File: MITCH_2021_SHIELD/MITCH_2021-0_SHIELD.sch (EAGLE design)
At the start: 1 part, among them U1 NUCLEO-F401RE-BOTTOM

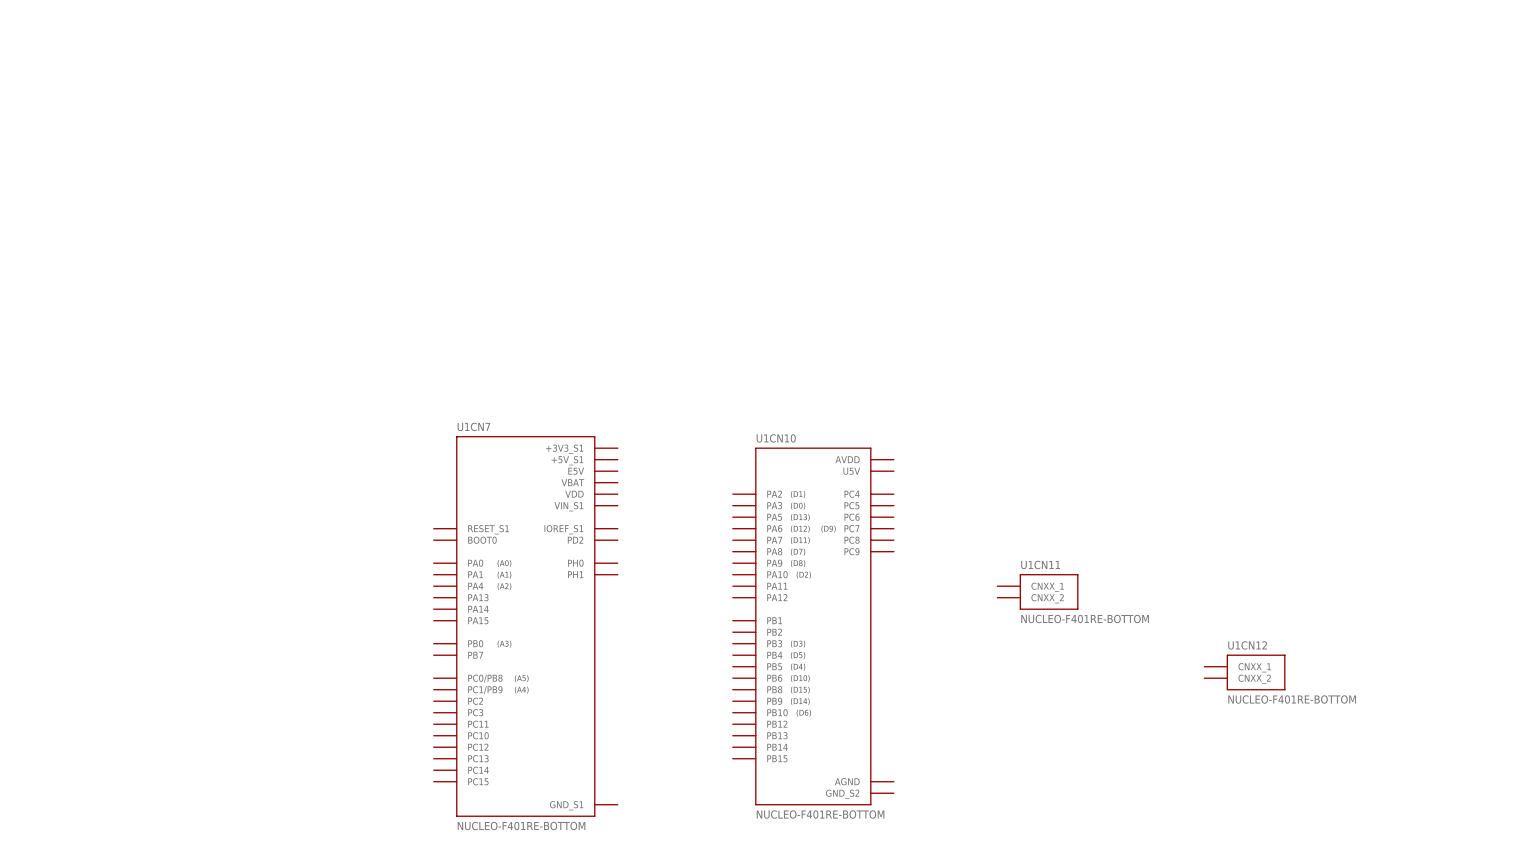
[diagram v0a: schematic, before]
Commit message: updated shield schematic
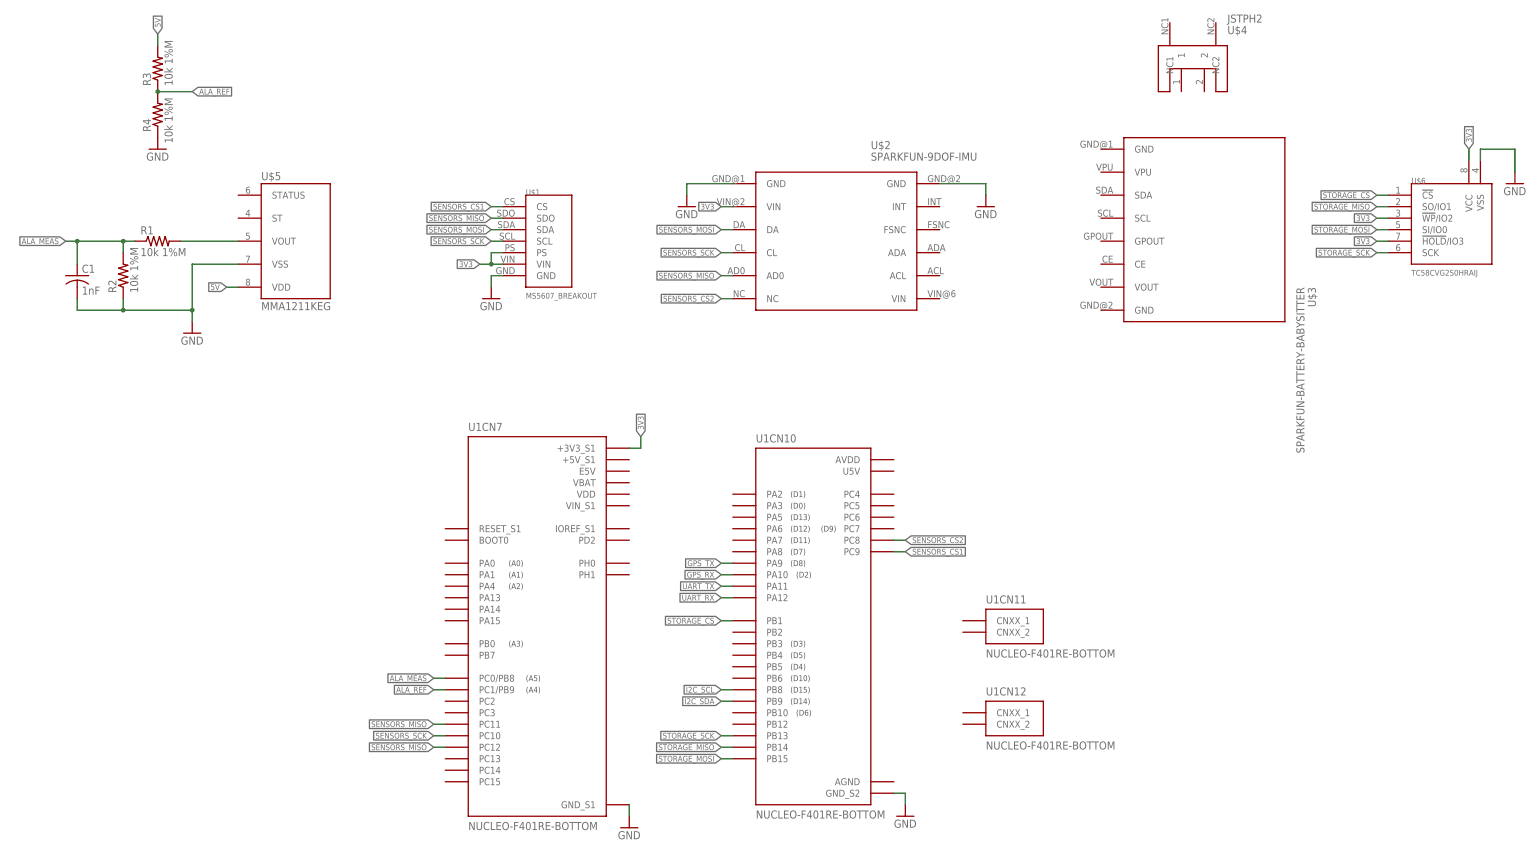
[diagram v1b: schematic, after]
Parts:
- added C1: 1nF, rcl:C-USC0805
- added R1, R2: 10k 1%M, rcl:R-US_M0805
- added R3, R4: 10k 1%M, resistor:R-US_R0805
- added U$1: MS5607_BREAKOUT, MITCH Shield:MS5607_BREAKOUT
- added U$2: SPARKFUN-9DOF-IMU, MITCH Shield:SPARKFUN-9DOF-IMU
- added U$3: SPARKFUN-BATTERY-BABYSITTER, MITCH Shield:SPARKFUN-BATTERY-BABYSITTER
- added U$4: JSTPH2, MITCH Shield:JSTPH2
- added U$5: MMA1211KEG, MITCH Shield:MMA1211KEG
- added U$6: TC58CVG2S0HRAIJ, MITCH Shield:TC58CVG2S0HRAIJ
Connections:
- new net 3V3: U$1.PS, U$1.VIN, U$2.VIN@2, U$6.!HOLD!/IO3, U$6.!WP!/IO2, U$6.VCC, U1CN7.+3V3_S1
- new net 5V: R3.2, U$5.VDD
- new net ALA_MEAS: C1.1, R1.1, R2.2, U1CN7.PC0/PB8
- new net ALA_REF: R3.1, R4.2, U1CN7.PC1/PB9
- new net GND: C1.2, R2.1, R4.1, U$1.GND, U$2.GND@1, U$2.GND@2, U$5.VSS, U$6.VSS, U1CN10.GND_S2, U1CN7.GND_S1
- new net GPS_RX: U1CN10.PA10
- new net GPS_TX: U1CN10.PA9
- new net I2C_SCL: U1CN10.PB8
- new net I2C_SDA: U1CN10.PB9
- new net N$2: R1.2, U$5.VOUT
- new net SENSORS_CS1: U$1.CS, U1CN10.PC9
- new net SENSORS_CS2: U$2.NC, U1CN10.PC8
- new net SENSORS_MISO: U$1.SDO, U$2.AD0, U1CN7.PC11, U1CN7.PC12
- new net SENSORS_MOSI: U$1.SDA, U$2.DA
- new net SENSORS_SCK: U$1.SCL, U$2.CL, U1CN7.PC10
- new net STORAGE_CS: U$6.!CS!, U1CN10.PB1
- new net STORAGE_MISO: U$6.SO/IO1, U1CN10.PB14
- new net STORAGE_MOSI: U$6.SI/IO0, U1CN10.PB15
- new net STORAGE_SCK: U$6.SCK, U1CN10.PB13
- new net UART_RX: U1CN10.PA12
- new net UART_TX: U1CN10.PA11
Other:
- moved on the sheet: U1CN11, U1CN12, U1CN7

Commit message: Further shield development
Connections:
- new net ALA_ST: U$5.ST, U1CN7.PC3
- new net ALA_STATUS: U$5.STATUS, U1CN7.PC2
- new net VBS: U$3.VOUT
- net 3V3: now also U$3.VPU
- net GND: now also U$3.GND@1, U$3.GND@2
- net I2C_SCL: now also U$3.SCL
- net I2C_SDA: now also U$3.SDA
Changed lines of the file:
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@@
 <part name="R3" library="resistor" library_urn="urn:adsk.eagle:library:348" deviceset="R-US_" device="R0805" package3d_urn="urn:adsk.eagle:package:23553/2" value="10k 1%M"/>
 <part name="GND20" library="supply1" library_urn="urn:adsk.eagle:library:371" deviceset="GND" device=""/>
+<part name="GND8" library="supply1" library_urn="urn:adsk.eagle:library:371" deviceset="GND" device=""/>
+<part name="GND9" library="supply1" library_urn="urn:adsk.eagle:library:371" deviceset="GND" device=""/>
 </parts>
 <sheets>
@@
 <attribute name="VALUE" x="-96.52" y="185.42" size="1.778" layer="96"/>
 </instance>
+<instance part="GND8" gate="1" x="104.14" y="182.88" smashed="yes">
+<attribute name="VALUE" x="101.6" y="180.34" size="1.778" layer="96"/>
+</instance>
+<instance part="GND9" gate="1" x="111.76" y="147.32" smashed="yes">
+<attribute name="VALUE" x="109.22" y="144.78" size="1.778" layer="96"/>
+</instance>
 </instances>
 <busses>
@@
 <wire x1="177.8" y1="167.64" x2="175.26" y2="167.64" width="0.1524" layer="91"/>
 <label x="175.26" y="167.64" size="1.27" layer="95" rot="R180" xref="yes"/>
+</segment>
+<segment>
+<pinref part="U$3" gate="G$1" pin="VPU"/>
+<wire x1="114.3" y1="182.88" x2="111.76" y2="182.88" width="0.1524" layer="91"/>
+<label x="111.76" y="182.88" size="1.27" layer="95" rot="R180" xref="yes"/>
 </segment>
 </net>
@@
 <pinref part="GND20" gate="1" pin="GND"/>
 </segment>
+<segment>
+<pinref part="U$3" gate="G$1" pin="GND@1"/>
+<wire x1="114.3" y1="187.96" x2="104.14" y2="187.96" width="0.1524" layer="91"/>
+<wire x1="104.14" y1="187.96" x2="104.14" y2="185.42" width="0.1524" layer="91"/>
+<pinref part="GND8" gate="1" pin="GND"/>
+</segment>
+<segment>
+<pinref part="U$3" gate="G$1" pin="GND@2"/>
+<wire x1="114.3" y1="152.4" x2="111.76" y2="152.4" width="0.1524" layer="91"/>
+<wire x1="111.76" y1="152.4" x2="111.76" y2="149.86" width="0.1524" layer="91"/>
+<pinref part="GND9" gate="1" pin="GND"/>
+</segment>
 </net>
 <net name="SENSORS_SCK" class="0">
@@
 <label x="30.48" y="68.58" size="1.27" layer="95" rot="R180" xref="yes"/>
 </segment>
+<segment>
+<pinref part="U$3" gate="G$1" pin="SCL"/>
+<wire x1="114.3" y1="172.72" x2="111.76" y2="172.72" width="0.1524" layer="91"/>
+<label x="111.76" y="172.72" size="1.27" layer="95" rot="R180" xref="yes"/>
+</segment>
 </net>
 <net name="I2C_SDA" class="0">
@@
 <wire x1="33.02" y1="66.04" x2="30.48" y2="66.04" width="0.1524" layer="91"/>
 <label x="30.48" y="66.04" size="1.27" layer="95" rot="R180" xref="yes"/>
+</segment>
+<segment>
+<pinref part="U$3" gate="G$1" pin="SDA"/>
+<wire x1="114.3" y1="177.8" x2="111.76" y2="177.8" width="0.1524" layer="91"/>
+<label x="111.76" y="177.8" size="1.27" layer="95" rot="R180" xref="yes"/>
 </segment>
 </net>
@@
 </segment>
 </net>
+<net name="ALA_STATUS" class="0">
+<segment>
+<pinref part="U1" gate="CN7" pin="PC2"/>
+<wire x1="-30.48" y1="66.04" x2="-33.02" y2="66.04" width="0.1524" layer="91"/>
+<label x="-33.02" y="66.04" size="1.27" layer="95" rot="R180" xref="yes"/>
+</segment>
+<segment>
+<pinref part="U$5" gate="G$1" pin="STATUS"/>
+<wire x1="-76.2" y1="177.8" x2="-78.74" y2="177.8" width="0.1524" layer="91"/>
+<label x="-78.74" y="177.8" size="1.27" layer="95" rot="R180" xref="yes"/>
+</segment>
+</net>
+<net name="ALA_ST" class="0">
+<segment>
+<pinref part="U1" gate="CN7" pin="PC3"/>
+<wire x1="-30.48" y1="63.5" x2="-33.02" y2="63.5" width="0.1524" layer="91"/>
+<label x="-33.02" y="63.5" size="1.27" layer="95" rot="R180" xref="yes"/>
+</segment>
+<segment>
+<pinref part="U$5" gate="G$1" pin="ST"/>
+<wire x1="-76.2" y1="172.72" x2="-78.74" y2="172.72" width="0.1524" layer="91"/>
+<label x="-78.74" y="172.72" size="1.27" layer="95" rot="R180" xref="yes"/>
+</segment>
+</net>
+<net name="VBS" class="0">
+<segment>
+<pinref part="U$3" gate="G$1" pin="VOUT"/>
+<wire x1="114.3" y1="157.48" x2="111.76" y2="157.48" width="0.1524" layer="91"/>
+<label x="111.76" y="157.48" size="1.27" layer="95" rot="R180" xref="yes"/>
+</segment>
+</net>

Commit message: added boost buck to mitch shield
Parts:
- removed U$4: JSTPH2, MITCH Shield:JSTPH2
- added C10: 10pF, rcl:C-USC0805
- added C7: (2*10)uF, rcl:C-USC0805
- added C8: (3*22)uF, rcl:C-USC0805
- added C9: 0.1uF, rcl:C-USC0805
- added IC1: TPS63060DSCT, SamacSys_Parts:TPS63060DSCT
- added L1: XFL4020-102MEB, SamacSys_Parts:XFL4020-102MEB
- added R5, R7: 1M, rcl:R-US_R0805
- added R6: 111k, rcl:R-US_R0805
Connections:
- new net FB: C10.1, IC1.FB, R5.1, R6.2
- new net L1: IC1.L1, L1.2
- new net L2: IC1.L2, L1.1
- new net PG: IC1.PG, R7.1
- new net VAUX: C9.1, IC1.VAUX
- net 5V: now also C8.1, IC1.VOUT, R5.2, R7.2
- net GND: now also C10.2, C7.2, C8.2, C9.2, IC1.EP/PGND_1, IC1.EP/PGND_2, IC1.EP/PGND_3, IC1.EP/PGND_4, IC1.EP/PGND_5, IC1.EP/PGND_6, IC1.EP/PGND_7, IC1.EP/PGND_8, IC1.EP/PGND_9, IC1.GND, IC1.PS/SYNC, R6.1
- net VBS: now also C7.1, IC1.EN, IC1.VIN

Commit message: Shield board stuff
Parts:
- removed U$6: TC58CVG2S0HRAIJ, MITCH Shield:TC58CVG2S0HRAIJ
- added U3: MS5607_BREAKOUT, MITCH Shield:MS5607_BREAKOUT
- U$1: value MS5607_BREAKOUT -> TC58CVG2S0HRAIJ-ACTUAL; device MITCH Shield:MS5607_BREAKOUT -> MITCH Shield:TC58CVG2S0HRAIJ-ACTUAL
- renumbered IC1 to U7, U$2 to U4, U$3 to U5, U$5 to U2
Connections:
- net 3V3: now also U$1.!HOLD!/IO3, U$1.!WP!/IO2, U$1.VCC, U3.PS, U3.VIN; no longer U$1.PS, U$1.VIN, U$6.!HOLD!/IO3, U$6.!WP!/IO2, U$6.VCC
- net GND: now also U$1.VSS, U3.GND; no longer U$1.GND, U$6.VSS
- net SENSORS_CS1: now also U3.CS; no longer U$1.CS
- net SENSORS_MISO: now also U3.SDO; no longer U$1.SDO
- net SENSORS_MOSI: now also U3.SDA; no longer U$1.SDA
- net SENSORS_SCK: now also U3.SCL; no longer U$1.SCL
- net STORAGE_CS: now also U$1.!CS!; no longer U$6.!CS!
- net STORAGE_MISO: now also U$1.SO/IO1; no longer U$6.SO/IO1
- net STORAGE_MOSI: now also U$1.SI/IO0; no longer U$6.SI/IO0
- net STORAGE_SCK: now also U$1.SCK; no longer U$6.SCK

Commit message: stuff
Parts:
- added JP1: (no value), pinhead:PINHD-1X5/90
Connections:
- net 5V: now also JP1.5
- net ALA_MEAS: now also JP1.3
- net ALA_ST: now also JP1.2
- net ALA_STATUS: now also JP1.1
- net GND: now also JP1.4
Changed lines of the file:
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@@
 <part name="GND23" library="supply1" library_urn="urn:adsk.eagle:library:371" deviceset="GND" device=""/>
 <part name="U$1" library="MITCH Shield" deviceset="TC58CVG2S0HRAIJ-ACTUAL" device=""/>
+<part name="JP1" library="pinhead" library_urn="urn:adsk.eagle:library:325" deviceset="PINHD-1X5" device="/90" package3d_urn="urn:adsk.eagle:package:22467/2"/>
+<part name="GND11" library="supply1" library_urn="urn:adsk.eagle:library:371" deviceset="GND" device=""/>
 </parts>
 <sheets>
@@
 <attribute name="NAME" x="182.88" y="180.34" size="1.27" layer="95"/>
 <attribute name="VALUE" x="182.88" y="160.02" size="1.27" layer="96"/>
+</instance>
+<instance part="JP1" gate="A" x="-63.5" y="132.08" smashed="yes">
+<attribute name="NAME" x="-69.85" y="140.335" size="1.778" layer="95"/>
+<attribute name="VALUE" x="-69.85" y="121.92" size="1.778" layer="96"/>
+</instance>
+<instance part="GND11" gate="1" x="-81.28" y="121.92" smashed="yes">
+<attribute name="VALUE" x="-83.82" y="119.38" size="1.778" layer="96"/>
 </instance>
 </instances>
@@
 <junction x="213.36" y="68.58"/>
 </segment>
+<segment>
+<pinref part="JP1" gate="A" pin="4"/>
+<wire x1="-66.04" y1="129.54" x2="-81.28" y2="129.54" width="0.1524" layer="91"/>
+<wire x1="-81.28" y1="129.54" x2="-81.28" y2="124.46" width="0.1524" layer="91"/>
+<pinref part="GND11" gate="1" pin="GND"/>
+</segment>
 </net>
 <net name="SENSORS_SCK" class="0">
@@
 <junction x="248.92" y="121.92"/>
 </segment>
+<segment>
+<pinref part="JP1" gate="A" pin="5"/>
+<wire x1="-66.04" y1="127" x2="-73.66" y2="127" width="0.1524" layer="91"/>
+<label x="-73.66" y="127" size="1.27" layer="95" rot="R180" xref="yes"/>
+</segment>
 </net>
 <net name="N$2" class="0">
@@
 <label x="-33.02" y="71.12" size="1.27" layer="95" rot="R180" xref="yes"/>
 </segment>
+<segment>
+<pinref part="JP1" gate="A" pin="3"/>
+<wire x1="-66.04" y1="132.08" x2="-73.66" y2="132.08" width="0.1524" layer="91"/>
+<label x="-73.66" y="132.08" size="1.27" layer="95" rot="R180" xref="yes"/>
+</segment>
 </net>
 <net name="ALA_REF" class="0">
@@
 <label x="-78.74" y="177.8" size="1.27" layer="95" rot="R180" xref="yes"/>
 </segment>
+<segment>
+<pinref part="JP1" gate="A" pin="1"/>
+<wire x1="-66.04" y1="137.16" x2="-73.66" y2="137.16" width="0.1524" layer="91"/>
+<label x="-137.16" y="177.8" size="1.27" layer="95"/>
+<label x="-73.66" y="137.16" size="1.27" layer="95" rot="R180" xref="yes"/>
+</segment>
 </net>
 <net name="ALA_ST" class="0">
@@
 <label x="-78.74" y="172.72" size="1.27" layer="95" rot="R180" xref="yes"/>
 </segment>
-</net>
+<segment>
+<pinref part="JP1" gate="A" pin="2"/>
+<wire x1="-66.04" y1="134.62" x2="-73.66" y2="134.62" width="0.1524" layer="91"/>
+<label x="-73.66" y="134.62" size="1.27" layer="95" rot="R180" xref="yes"/>
+</segment>
+</net>

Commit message: Routed most of mitch shield
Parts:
- removed C1: 1nF, rcl:C-USC0805
- removed JP1: (no value), pinhead:PINHD-1X5/90
- removed R1, R2: 10k 1%M, rcl:R-US_M0805
- removed R3, R4: 10k 1%M, resistor:R-US_R0805
- removed U2: MMA1211KEG, MITCH Shield:MMA1211KEG
- added J1, J2: 22-27-2021-02, con-molex:22-27-2021-02
- added S1: (no value), switch-omron:10-XX
- added X1: (no value), con-molex:22-23-2061
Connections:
- removed net N$2: R1.2, U2.VOUT
- new net N$1: U1CN12.CNXX_1, U1CN12.CNXX_2
- new net N$3: U1CN11.CNXX_1, U1CN11.CNXX_2
- new net N$4: S1.S1, U5.CE
- new net VBS_SWITCH: C7.1, J2-1.S, U7.EN, U7.VIN
- net 3V3: no longer U3.PS
- net 5V: now also U1CN7.E5V, X1-5.S; no longer JP1.5, R3.2, U2.VDD
- net ALA_MEAS: now also X1-1.S; no longer C1.1, JP1.3, R1.1, R2.2
- net ALA_REF: now also X1-2.S; no longer R3.1, R4.2
- net ALA_ST: now also X1-3.S; no longer JP1.2, U2.ST
- net ALA_STATUS: now also X1-4.S; no longer JP1.1, U2.STATUS
- net GND: now also J1-2.S, J2-2.S, S1.P1, U3.PS, X1-6.S; no longer C1.2, JP1.4, R2.1, R4.1, U2.VSS
- net SENSORS_CS1: now also U1CN10.PC8; no longer U1CN10.PC9
- net SENSORS_CS2: now also U1CN10.PC9; no longer U1CN10.PC8
- net SENSORS_MISO: no longer U1CN7.PC12
- net SENSORS_MOSI: now also U1CN7.PC12
- net VBS: now also J1-1.S; no longer C7.1, U7.EN, U7.VIN
